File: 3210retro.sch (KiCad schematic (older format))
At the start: 10 parts, among them P102 BAT, P103 DC, P105 EAR, P109 RUMBLE, X101 ANT_GPS, X102 ANT_GSM

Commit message: Added boost converter to battery circuit
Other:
- moved on the sheet: P102, P103, R?
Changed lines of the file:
@@
 LIBS:sn74avc2t244
 LIBS:WM8960CGEFL
+LIBS:tps61021a
 LIBS:3210retro-cache
 EELAYER 25 0
@@
 $EndDescr
 $Sheet
-S 2500 3400 1750 1200
+S 2200 3400 1750 1200
 U 5805F477
 F0 "Power and Battery" 60
 F1 "POWER.sch" 60
-F2 "VBAT+" I L 2500 3700 60
-F3 "VBAT-" I L 2500 3800 60
-F4 "V_USB_BUS" I L 2500 4500 60
-F5 "VDC+" I L 2500 4100 60
-F6 "VDC-" I L 2500 4200 60
-F7 "VBAT_ref" O R 4250 3700 60
-F8 "V_USB_BUS_ref" O R 4250 3800 60
-F9 "VDC_ref" O R 4250 3900 60
-F10 "~CHARGING" O R 4250 4200 60
-$EndSheet
-$Sheet
-S 1750 7450 1100 1250
+F2 "VBAT+" I L 2200 3700 60
+F3 "VBAT-" I L 2200 3800 60
+F4 "V_USB_BUS" I L 2200 4500 60
+F5 "VDC+" I L 2200 4100 60
+F6 "VDC-" I L 2200 4200 60
+F7 "VBAT_ref" O R 3950 3700 60
+F8 "V_USB_BUS_ref" O R 3950 3800 60
+F9 "VDC_ref" O R 3950 3900 60
+F10 "~CHARGING" O R 3950 4200 60
+$EndSheet
+$Sheet
+S 1450 7450 1100 1250
 U 5805F4C1
 F0 "Display" 60
 F1 "DISPLAY.sch" 60
-F2 "LCD_DATA[0..23]" I R 2850 8000 60
-F3 "LCD_CLK" I R 2850 7900 60
-F4 "LCD_HSYNC" I R 2850 8100 60
-F5 "LCD_VSYNC" I R 2850 8200 60
-F6 "LCD_ENABLE" I R 2850 8300 60
-F7 "LCD_RESET" I R 2850 8400 60
+F2 "LCD_DATA[0..23]" I R 2550 8000 60
+F3 "LCD_CLK" I R 2550 7900 60
+F4 "LCD_HSYNC" I R 2550 8100 60
+F5 "LCD_VSYNC" I R 2550 8200 60
+F6 "LCD_ENABLE" I R 2550 8300 60
+F7 "LCD_RESET" I R 2550 8400 60
 $EndSheet
 $Comp
 L CONN_01X02 P102
 U 1 1 580667EA
-P 2000 3750
-F 0 "P102" H 2000 3900 50  0000 C CNN
-F 1 "BAT" V 2100 3750 50  0000 C CNN
-F 2 "Pin_Headers:Pin_Header_Straight_2x01" H 2000 3750 50  0001 C CNN
-F 3 "" H 2000 3750 50  0000 C CNN
-	1    2000 3750
+P 1700 3750
+F 0 "P102" H 1700 3900 50  0000 C CNN
+F 1 "BAT" V 1800 3750 50  0000 C CNN
+F 2 "Pin_Headers:Pin_Header_Straight_2x01" H 1700 3750 50  0001 C CNN
+F 3 "" H 1700 3750 50  0000 C CNN
+	1    1700 3750
 	-1   0    0    1
 $EndComp
 Wire Wire Line
-	2500 3800 2200 3800
-Wire Wire Line
-	2200 3700 2500 3700
+	2200 3800 1900 3800
+Wire Wire Line
+	1900 3700 2200 3700
 $Sheet
 S 13200 3400 1400 3700
@@
 F26 "SPK_LP" O R 14600 3900 60
 F27 "SPK_LN" O R 14600 4000 60
+F28 "SPK_+" I L 13200 3500 60
+F29 "SPK_-" I L 13200 3600 60
 $EndSheet
 $Comp
@@
 L GND #PWR02
 U 1 1 580BB0C9
-P 2300 6150
-F 0 "#PWR02" H 2300 5900 50  0001 C CNN
-F 1 "GND" H 2300 6000 50  0000 C CNN
-F 2 "" H 2300 6150 50  0000 C CNN
-F 3 "" H 2300 6150 50  0000 C CNN
-	1    2300 6150
-	1    0    0    -1
-$EndComp
-Wire Wire Line
-	2300 5450 2300 6150
-Wire Wire Line
-	2300 5450 2250 5450
-Wire Wire Line
-	1850 5650 1850 5700
-Connection ~ 2300 6100
-Wire Wire Line
-	2350 5050 2250 5050
-Wire Wire Line
-	2350 4500 2350 5050
-Wire Wire Line
-	2350 4500 2500 4500
+P 2000 6150
+F 0 "#PWR02" H 2000 5900 50  0001 C CNN
+F 1 "GND" H 2000 6000 50  0000 C CNN
+F 2 "" H 2000 6150 50  0000 C CNN
+F 3 "" H 2000 6150 50  0000 C CNN
+	1    2000 6150
+	1    0    0    -1
+$EndComp
+Wire Wire Line
+	2000 5450 2000 6150
+Wire Wire Line
+	2000 5450 1950 5450
+Wire Wire Line
+	1550 5650 1550 5700
+Connection ~ 2000 6100
+Wire Wire Line
+	2050 5050 1950 5050
+Wire Wire Line
+	2050 4500 2050 5050
+Wire Wire Line
+	2050 4500 2200 4500
 $Comp
 L CONN_01X02 P103
 U 1 1 580C5E12
-P 2000 4150
-F 0 "P103" H 2000 4300 50  0000 C CNN
-F 1 "DC" V 2100 4150 50  0000 C CNN
-F 2 "Pin_Headers:Pin_Header_Straight_2x01" H 2000 4150 50  0001 C CNN
-F 3 "" H 2000 4150 50  0000 C CNN
-	1    2000 4150
+P 1700 4150
+F 0 "P103" H 1700 4300 50  0000 C CNN
+F 1 "DC" V 1800 4150 50  0000 C CNN
+F 2 "Pin_Headers:Pin_Header_Straight_2x01" H 1700 4150 50  0001 C CNN
+F 3 "" H 1700 4150 50  0000 C CNN
+	1    1700 4150
 	-1   0    0    1
 $EndComp
 Wire Wire Line
-	4250 4200 5950 4200
-Wire Wire Line
-	2200 4100 2500 4100
-Wire Wire Line
-	2500 4200 2200 4200
-Wire Wire Line
-	5950 5350 2250 5350
-Wire Wire Line
-	2250 5250 5950 5250
-Wire Wire Line
-	5950 5150 2250 5150
+	3950 4200 5650 4200
+Wire Wire Line
+	1900 4100 2200 4100
+Wire Wire Line
+	2200 4200 1900 4200
+Wire Wire Line
+	5650 5350 1950 5350
+Wire Wire Line
+	1950 5250 5650 5250
+Wire Wire Line
+	5650 5150 1950 5150
 $Sheet
 S 10500 2650 1650 1750
@@
 Text Notes 10550 4350 0    98   ~ 0
 5
-Text Notes 2700 8650 0    98   ~ 0
+Text Notes 2400 8650 0    98   ~ 0
 3
 Wire Notes Line
-	2500 5050 2500 5300
+	2200 5050 2200 5300
 Wire Notes Line
-	2500 5300 5850 5300
+	2200 5300 5550 5300
 Wire Notes Line
-	5850 5300 5850 5050
+	5550 5300 5550 5050
 Wire Notes Line
-	5850 5050 2500 5050
-Text Notes 2550 5150 0    59   ~ 0
+	5550 5050 2200 5050
+Text Notes 2250 5150 0    59   ~ 0
 50Ohm
 Wire Wire Line
@@
 L USB_OTG P?
 U 1 1 594309F1
-P 1950 5250
-F 0 "P?" H 2275 5125 50  0000 C CNN
-F 1 "USB_OTG" H 1950 5450 50  0000 C CNN
-F 2 "" V 1900 5150 50  0000 C CNN
-F 3 "" V 1900 5150 50  0000 C CNN
-	1    1950 5250
+P 1650 5250
+F 0 "P?" H 1975 5125 50  0000 C CNN
+F 1 "USB_OTG" H 1650 5450 50  0000 C CNN
+F 2 "" V 1600 5150 50  0000 C CNN
+F 3 "" V 1600 5150 50  0000 C CNN
+	1    1650 5250
 	0    -1   1    0
 $EndComp
@@
 L R R?
 U 1 1 5943206D
-P 1850 5850
-F 0 "R?" V 1930 5850 50  0000 C CNN
-F 1 "0" V 1850 5850 50  0000 C CNN
-F 2 "" V 1780 5850 50  0000 C CNN
-F 3 "" H 1850 5850 50  0000 C CNN
-	1    1850 5850
-	1    0    0    -1
-$EndComp
-Wire Wire Line
-	2300 6100 1850 6100
-Wire Wire Line
-	1850 6100 1850 6000
+P 1550 5850
+F 0 "R?" V 1630 5850 50  0000 C CNN
+F 1 "0" V 1550 5850 50  0000 C CNN
+F 2 "" V 1480 5850 50  0000 C CNN
+F 3 "" H 1550 5850 50  0000 C CNN
+	1    1550 5850
+	1    0    0    -1
+$EndComp
+Wire Wire Line
+	2000 6100 1550 6100
+Wire Wire Line
+	1550 6100 1550 6000
 Wire Bus Line
 	7650 4700 12900 4700
@@
 	7650 4800 7850 4800
 Wire Wire Line
-	2850 8400 5950 8400
-Wire Wire Line
-	5950 8300 2850 8300
-Wire Wire Line
-	2850 8200 5950 8200
-Wire Wire Line
-	5950 8100 2850 8100
-Wire Wire Line
-	2850 7900 5950 7900
-Wire Bus Line
-	5950 8000 2850 8000
+	2550 8400 5650 8400
+Wire Wire Line
+	5650 8300 2550 8300
+Wire Wire Line
+	2550 8200 5650 8200
+Wire Wire Line
+	5650 8100 2550 8100
+Wire Wire Line
+	2550 7900 5650 7900
+Wire Bus Line
+	5650 8000 2550 8000
 Wire Bus Line
 	9000 5550 7650 5550
@@
 NoConn ~ 7850 4800
 Wire Wire Line
-	5950 3700 4250 3700
-Wire Wire Line
-	4250 3800 5950 3800
-Wire Wire Line
-	5950 3900 4250 3900
+	5650 3700 3950 3700
+Wire Wire Line
+	3950 3800 5650 3800
+Wire Wire Line
+	5650 3900 3950 3900
 Wire Wire Line
 	14750 4700 14750 4750
 $Sheet
-S 5950 3100 1700 5800
+S 5650 3100 2000 5800
 U 5805F47D
 F0 "Controller" 60
 F1 "MCU.sch" 60
 F2 "~ON" I R 7650 8600 60
-F3 "D+" B L 5950 5250 60
-F4 "D-" B L 5950 5150 60
-F5 "USB_OTG_ID" O L 5950 5350 60
-F6 "VBAT_ref" I L 5950 3700 60
-F7 "V_USB_BUS_ref" I L 5950 3800 60
-F8 "VDC_ref" I L 5950 3900 60
-F9 "~CHARGING" I L 5950 4200 60
+F3 "D+" B L 5650 5250 60
+F4 "D-" B L 5650 5150 60
+F5 "USB_OTG_ID" O L 5650 5350 60
+F6 "VBAT_ref" I L 5650 3700 60
+F7 "V_USB_BUS_ref" I L 5650 3800 60
+F8 "VDC_ref" I L 5650 3900 60
+F9 "~CHARGING" I L 5650 4200 60
 F10 "GPS_TX" I R 7650 4000 60
 F11 "AT_UART[0..3]" B R 7650 3600 60
@@
 F17 "SAI1[0..6]" B R 7650 4700 60
 F18 "SAI2[0..3]" B R 7650 4800 60
-F19 "LCD_DATA[0..23]" O L 5950 8000 60
-F20 "LCD_CLK" O L 5950 7900 60
-F21 "LCD_ENABLE" O L 5950 8300 60
-F22 "LCD_HSYNC" O L 5950 8100 60
-F23 "LCD_VSYNC" O L 5950 8200 60
-F24 "LCD_RESET" O L 5950 8400 60
+F19 "LCD_DATA[0..23]" O L 5650 8000 60
+F20 "LCD_CLK" O L 5650 7900 60
+F21 "LCD_ENABLE" O L 5650 8300 60
+F22 "LCD_HSYNC" O L 5650 8100 60
+F23 "LCD_VSYNC" O L 5650 8200 60
+F24 "LCD_RESET" O L 5650 8400 60
 F25 "SD2_BUS[0..8]" B R 7650 5550 60
 F26 "BT_EN" O R 7650 5900 60

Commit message: reverting to old sheet structure
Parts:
- P?: symbol USB_OTG -> USB_OTG-RESCUE-3210retro
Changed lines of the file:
@@
 EESchema Schematic File Version 2
+LIBS:3210retro-rescue
 LIBS:power
 LIBS:device
@@
 LIBS:mtfc8gacaeam-1m_wt
 LIBS:sn74avc2t244
-LIBS:WM8960CGEFL
-LIBS:tps61021a
+LIBS:lsm9ds1
 LIBS:3210retro-cache
 EELAYER 25 0
@@
 	12200 7750 7650 7750
 $Comp
-L USB_OTG P?
+L USB_OTG-RESCUE-3210retro P?
 U 1 1 594309F1
 P 1650 5250

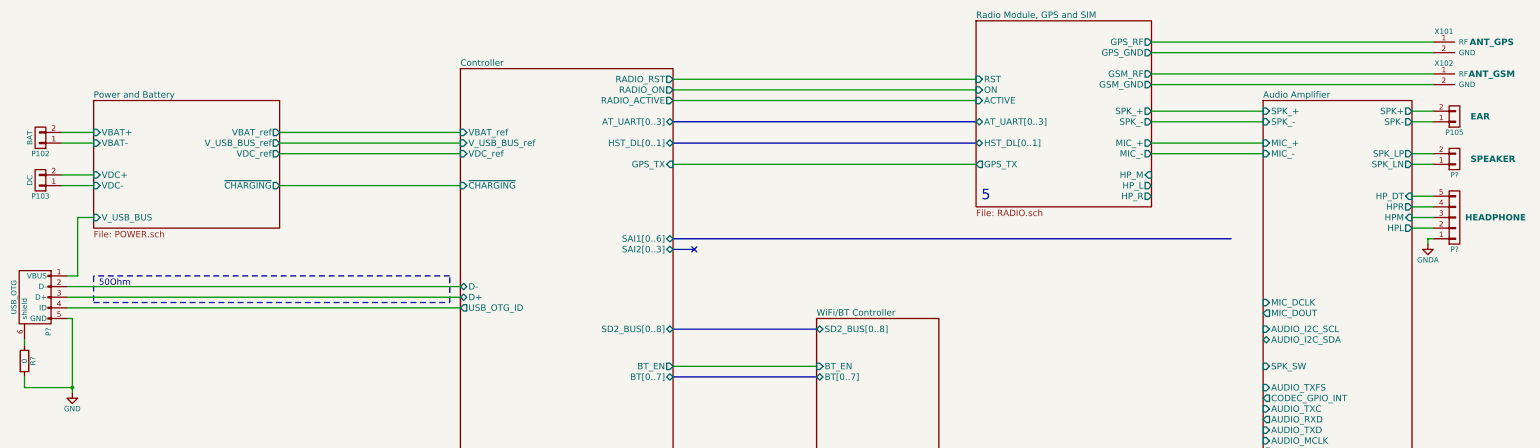
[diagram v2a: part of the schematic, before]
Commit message: Prepare for two battery types NiMH battery for using the original battery pack LiPo battery for using long lasting modern battery
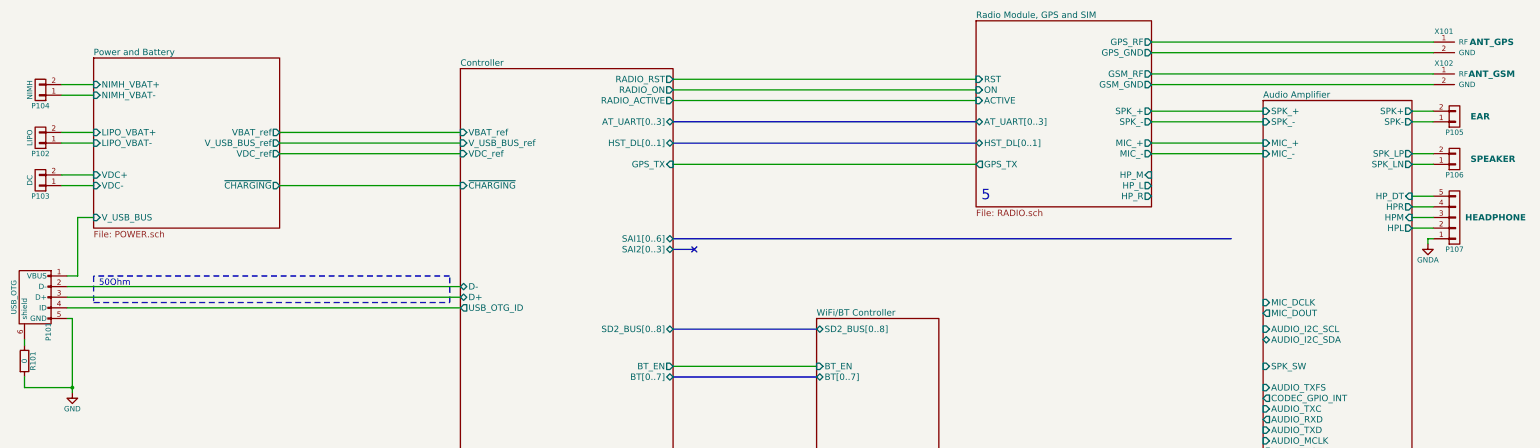
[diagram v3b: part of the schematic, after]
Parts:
- added P104: NIMH, Pin_Headers:Pin_Header_Straight_2x01, symbol CONN_01X02
- P102: value BAT -> LIPO
- gave numbers to parts that had none: 4
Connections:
- net Power and Battery/VBAT+ renamed Power and Battery/LIPO_VBAT+
- net Power and Battery/VBAT- renamed Power and Battery/LIPO_VBAT-
- new net Power and Battery/NIMH_VBAT+: P104.2 (P2)
- new net Power and Battery/NIMH_VBAT-: P104.1 (P1)
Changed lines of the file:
@@
 EESchema Schematic File Version 2
-LIBS:3210retro-rescue
-LIBS:power
-LIBS:device
-LIBS:transistors
-LIBS:conn
-LIBS:linear
-LIBS:regul
-LIBS:74xx
-LIBS:cmos4000
-LIBS:adc-dac
-LIBS:memory
-LIBS:xilinx
-LIBS:microcontrollers
-LIBS:dsp
-LIBS:microchip
-LIBS:analog_switches
-LIBS:motorola
-LIBS:texas
-LIBS:intel
-LIBS:audio
-LIBS:interface
-LIBS:digital-audio
-LIBS:philips
-LIBS:display
-LIBS:cypress
-LIBS:siliconi
-LIBS:opto
-LIBS:atmel
-LIBS:contrib
-LIBS:valves
 LIBS:a7
 LIBS:ft232rl
@@
 LIBS:sn74avc2t244
 LIBS:lsm9ds1
+LIBS:WM8960CGEFL
+LIBS:tps61021a
+LIBS:bq24400
+LIBS:power
+LIBS:device
+LIBS:transistors
+LIBS:conn
+LIBS:linear
+LIBS:regul
+LIBS:74xx
+LIBS:cmos4000
+LIBS:adc-dac
+LIBS:memory
+LIBS:xilinx
+LIBS:microcontrollers
+LIBS:dsp
+LIBS:microchip
+LIBS:analog_switches
+LIBS:motorola
+LIBS:texas
+LIBS:intel
+LIBS:audio
+LIBS:interface
+LIBS:digital-audio
+LIBS:philips
+LIBS:display
+LIBS:cypress
+LIBS:siliconi
+LIBS:opto
+LIBS:atmel
+LIBS:contrib
+LIBS:valves
 LIBS:3210retro-cache
 EELAYER 25 0
@@
 $EndDescr
 $Sheet
-S 2200 3400 1750 1200
+S 2200 3000 1750 1600
 U 5805F477
 F0 "Power and Battery" 60
 F1 "POWER.sch" 60
-F2 "VBAT+" I L 2200 3700 60
-F3 "VBAT-" I L 2200 3800 60
-F4 "V_USB_BUS" I L 2200 4500 60
-F5 "VDC+" I L 2200 4100 60
-F6 "VDC-" I L 2200 4200 60
-F7 "VBAT_ref" O R 3950 3700 60
-F8 "V_USB_BUS_ref" O R 3950 3800 60
-F9 "VDC_ref" O R 3950 3900 60
-F10 "~CHARGING" O R 3950 4200 60
+F2 "V_USB_BUS" I L 2200 4500 60
+F3 "VDC+" I L 2200 4100 60
+F4 "VDC-" I L 2200 4200 60
+F5 "VBAT_ref" O R 3950 3700 60
+F6 "V_USB_BUS_ref" O R 3950 3800 60
+F7 "VDC_ref" O R 3950 3900 60
+F8 "~CHARGING" O R 3950 4200 60
+F9 "NIMH_VBAT+" I L 2200 3250 60
+F10 "NIMH_VBAT-" I L 2200 3350 60
+F11 "LIPO_VBAT+" I L 2200 3700 60
+F12 "LIPO_VBAT-" I L 2200 3800 60
 $EndSheet
 $Sheet
@@
 P 1700 3750
 F 0 "P102" H 1700 3900 50  0000 C CNN
-F 1 "BAT" V 1800 3750 50  0000 C CNN
+F 1 "LIPO" V 1800 3750 50  0000 C CNN
 F 2 "Pin_Headers:Pin_Header_Straight_2x01" H 1700 3750 50  0001 C CNN
 F 3 "" H 1700 3750 50  0000 C CNN
@@
 	14600 3600 14800 3600
 $Comp
-L GNDA #PWR01
+L GNDA #PWR102
 U 1 1 58075318
 P 14750 4750
-F 0 "#PWR01" H 14750 4500 50  0001 C CNN
+F 0 "#PWR102" H 14750 4500 50  0001 C CNN
 F 1 "GNDA" H 14750 4600 50  0000 C CNN
 F 2 "" H 14750 4750 50  0000 C CNN
@@
 	7650 3300 10500 3300
 $Comp
-L GND #PWR02
+L GND #PWR101
 U 1 1 580BB0C9
 P 2000 6150
-F 0 "#PWR02" H 2000 5900 50  0001 C CNN
+F 0 "#PWR101" H 2000 5900 50  0001 C CNN
 F 1 "GND" H 2000 6000 50  0000 C CNN
 F 2 "" H 2000 6150 50  0000 C CNN
@@
 	12200 7750 7650 7750
 $Comp
-L USB_OTG-RESCUE-3210retro P?
+L USB_OTG-RESCUE-3210retro P101
 U 1 1 594309F1
 P 1650 5250
-F 0 "P?" H 1975 5125 50  0000 C CNN
+F 0 "P101" H 1975 5125 50  0000 C CNN
 F 1 "USB_OTG" H 1650 5450 50  0000 C CNN
 F 2 "" V 1600 5150 50  0000 C CNN
@@
 $EndComp
 $Comp
-L R R?
+L R R101
 U 1 1 5943206D
 P 1550 5850
-F 0 "R?" V 1630 5850 50  0000 C CNN
+F 0 "R101" V 1630 5850 50  0000 C CNN
 F 1 "0" V 1550 5850 50  0000 C CNN
 F 2 "" V 1480 5850 50  0000 C CNN
@@
 $EndSheet
 $Comp
-L CONN_01X02 P?
+L CONN_01X02 P106
 U 1 1 594B3CF4
 P 15000 3950
-F 0 "P?" H 15000 4100 50  0000 C CNN
+F 0 "P106" H 15000 4100 50  0000 C CNN
 F 1 "SPEAKER" H 15150 3950 60  0000 L CNB
 F 2 "Pin_Headers:Pin_Header_Straight_2x01" H 15000 3950 50  0001 C CNN
@@
 	14600 4000 14800 4000
 $Comp
-L CONN_01X05 P?
+L CONN_01X05 P107
 U 1 1 59452B57
 P 15000 4500
-F 0 "P?" H 15000 4800 50  0000 C CNN
+F 0 "P107" H 15000 4800 50  0000 C CNN
 F 1 "HEADPHONE" H 15100 4500 59  0000 L CNB
 F 2 "" H 15000 4500 50  0000 C CNN
@@
 Wire Wire Line
 	10500 3200 7650 3200
+$Comp
+L CONN_01X02 P104
+U 1 1 5956D99A
+P 1700 3300
+F 0 "P104" H 1700 3450 50  0000 C CNN
+F 1 "NIMH" V 1800 3300 50  0000 C CNN
+F 2 "Pin_Headers:Pin_Header_Straight_2x01" H 1700 3300 50  0001 C CNN
+F 3 "" H 1700 3300 50  0000 C CNN
+	1    1700 3300
+	-1   0    0    1
+$EndComp
+Wire Wire Line
+	2200 3350 1900 3350
+Wire Wire Line
+	1900 3250 2200 3250
 $EndSCHEMATC

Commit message: Modified power nets Added table of contents
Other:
- note added: "1"
- note added: "10"
- note added: "11"
- note added: "12"
- note added: "13"
- note added: "2"
- note added: "4"
- note added: "6"
- note added: "7"
- note added: "8"
- note added: "8,9,10,11,12,13"
- note added: "9"
- note added: "A7 radio module (GSM/GPRS/GPS)"
- note added: "Audio interface"
- note added: "Battery selection and power domain overview"
- note added: "Buttons & LEDs"
- note added: "CPU mainsheet"
- note added: "DDR3 RAM"
- note added: "Display interface"
- note added: "SD interface / eMMC"
- note added: "Top sheet"
- note added: "USB / IMU (gyro, accel, comp)"
- note added: "WiFi / Bluetooth"
- note added: "i.MX7 PMIC"
- note added: "i.MX7 power"
- moved on the sheet: P101, P102, P103, P104, P105, P106, P107, P109, R101, X101, X102
